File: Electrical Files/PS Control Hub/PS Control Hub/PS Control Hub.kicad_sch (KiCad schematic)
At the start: 0 parts

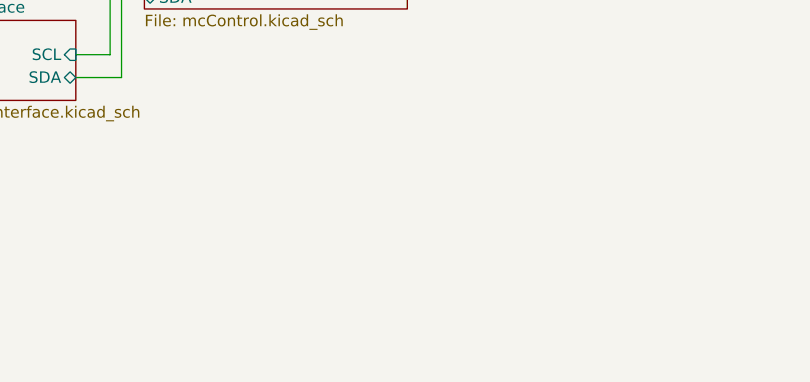
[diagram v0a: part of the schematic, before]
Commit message: Control Hub Housing, H&S PCB
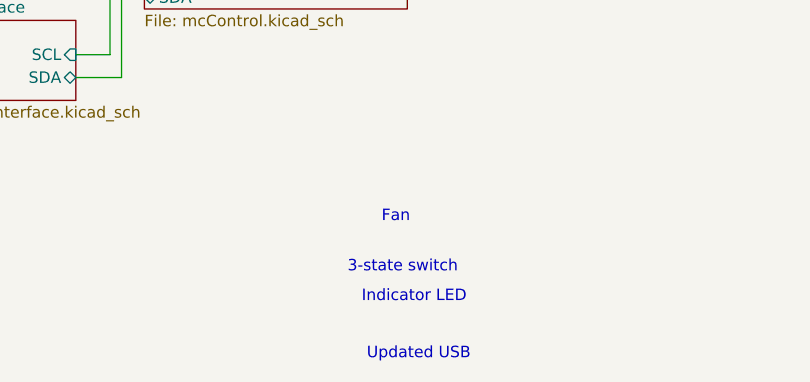
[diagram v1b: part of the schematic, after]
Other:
- note added: "3-state switch"
- note added: "Fan"
- note added: "Indicator LED"
- note added: "Updated USB"
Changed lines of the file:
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@@
 	(generator_version "9.0")
 	(paper "A4")
+	(text "Updated USB"
+		(exclude_from_sim no)
+		(at 128.27 115.824 0)
+		(effects
+			(font
+				(size 1.27 1.27)
+			)
+		)
+	)
+	(text "Fan"
+		(exclude_from_sim no)
+		(at 125.73 100.584 0)
+		(effects
+			(font
+				(size 1.27 1.27)
+			)
+		)
+	)
+	(text "Indicator LED"
+		(exclude_from_sim no)
+		(at 127.762 109.474 0)
+		(effects
+			(font
+				(size 1.27 1.27)
+			)
+		)
+	)
+	(text "3-state switch"
+		(exclude_from_sim no)
+		(at 126.492 106.172 0)
+		(effects
+			(font
+				(size 1.27 1.27)
+			)
+		)
+	)
 	(wire
 		(pts

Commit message: Control Hub, Flexible Hotplate, Housing Fan
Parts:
- added H1, H2, H3, H4: MountingHole_Pad, MountingHole:MountingHole_3.2mm_M3_DIN965_Pad_TopBottom, symbol Mechanical:MountingHole_Pad
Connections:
- no-connect marks 0 -> 4
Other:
- sheet MC Control ports: added none; removed 5VDC
- sheet Power Management ports: added 24VDC; removed 5VDC
